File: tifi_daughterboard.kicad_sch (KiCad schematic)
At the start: 16 parts

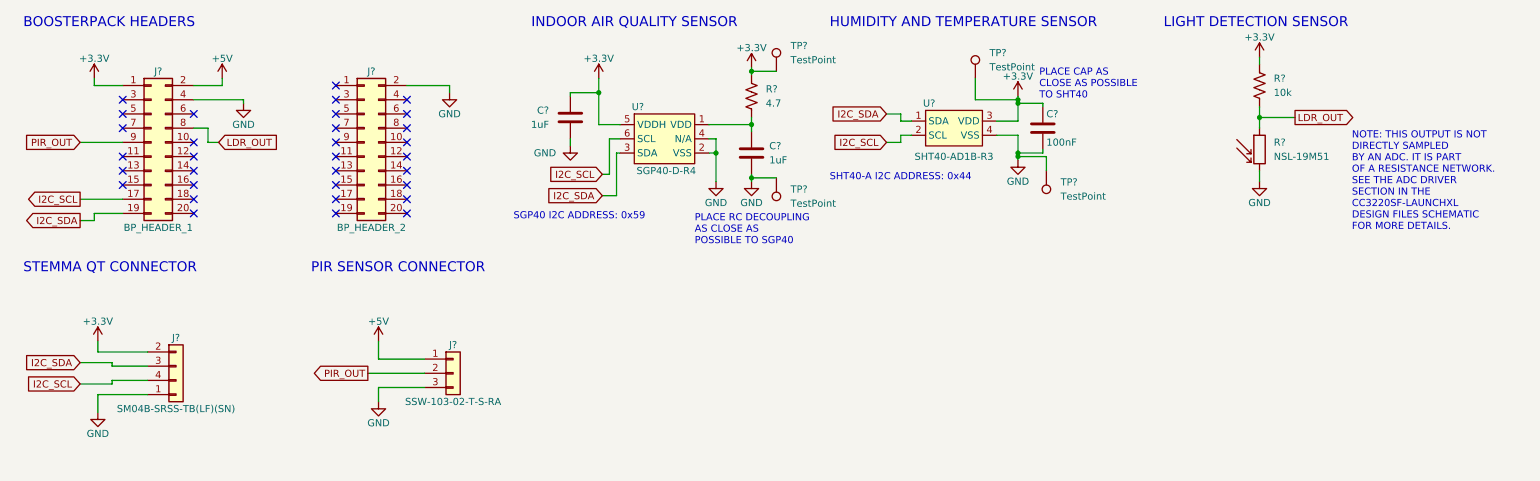
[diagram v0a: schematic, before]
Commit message: Generic cleanup.
Removed test points temporarily until schematic is feature-complete.
Added PWR_FLAG to BoosterPack power pins for ERC check.
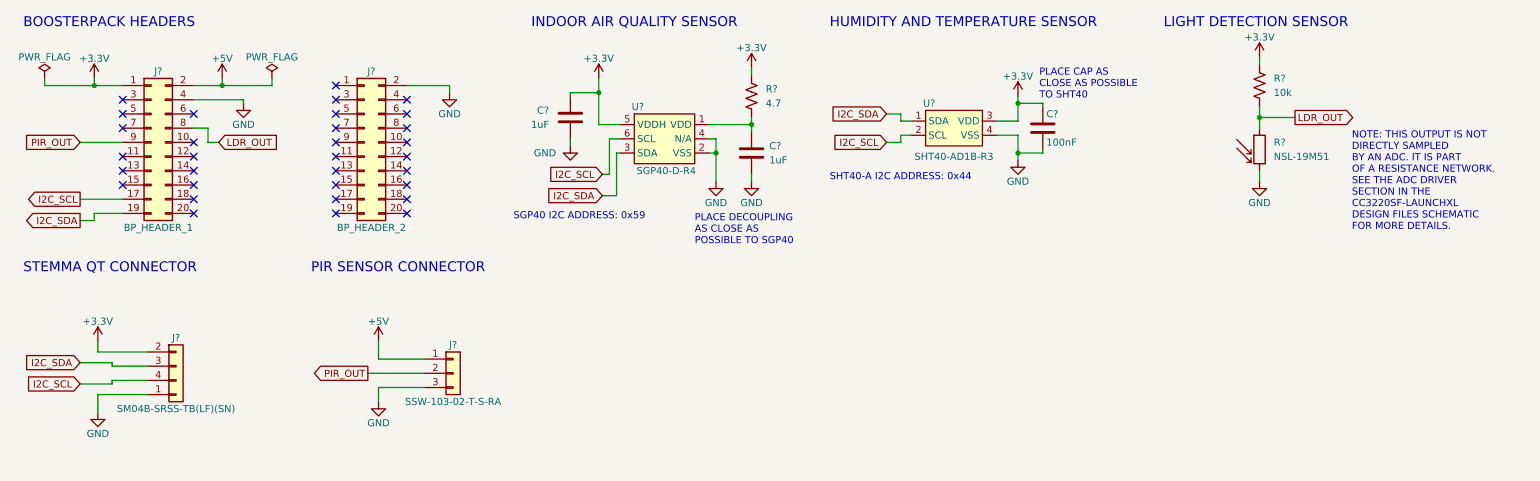
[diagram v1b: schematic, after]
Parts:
- removed TP? (x4): TestPoint, TestPoint:TestPoint_THTPad_1.0x1.0mm_Drill0.5mm, symbol Connector:TestPoint
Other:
- note added: "PLACE DECOUPLING AS CLOSE AS POSSIBLE TO SGP40"
- note removed: "PLACE RC DECOUPLING AS CLOSE AS POSSIBLE TO SGP40"

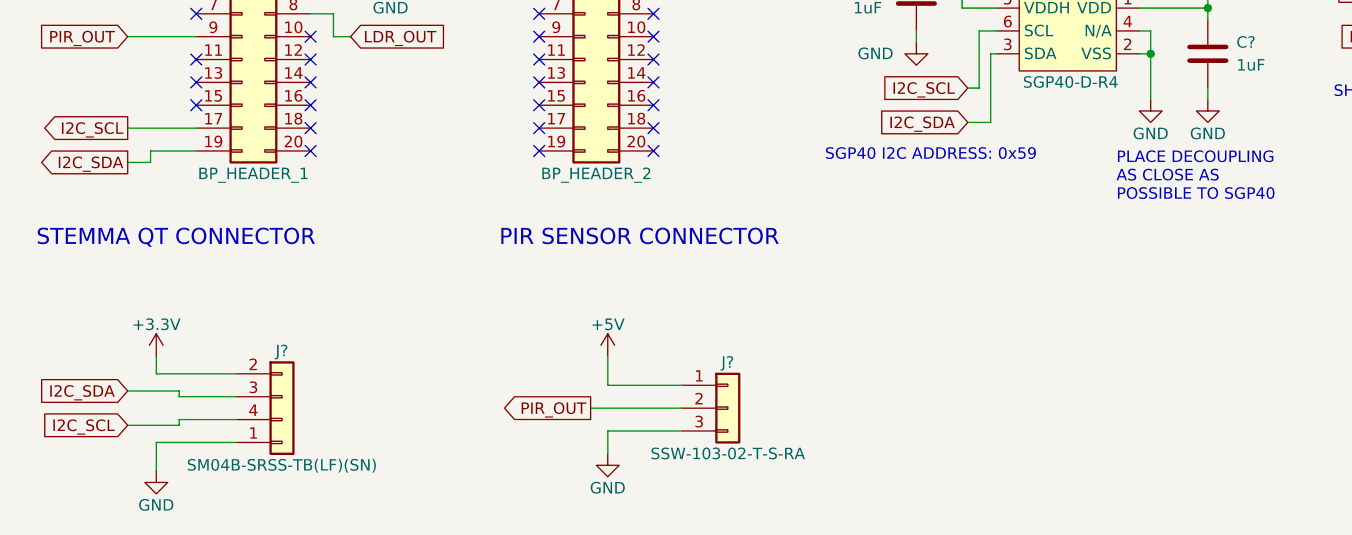
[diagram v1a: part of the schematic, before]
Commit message: Assign parts to BP headers. Add power LED.
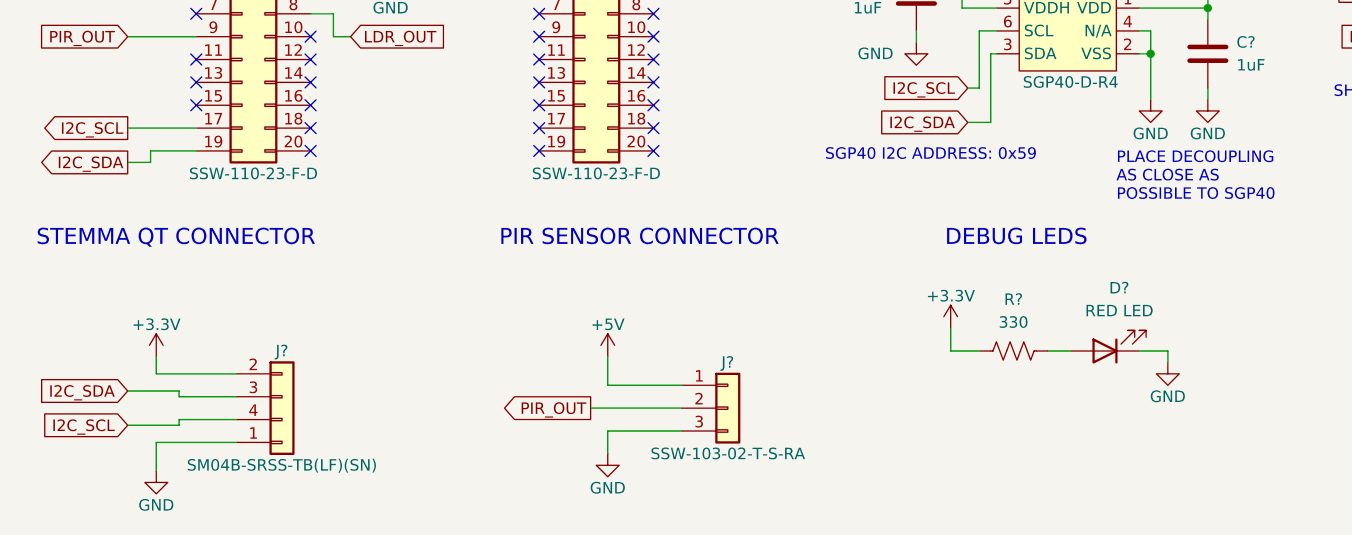
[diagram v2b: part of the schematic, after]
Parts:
- added D?: RED LED, LED_SMD:LED_0805_2012Metric_Pad1.15x1.40mm_HandSolder, symbol Device:LED
- added R?: 330, symbol Device:R_US
- J?: value BP_HEADER_2 -> SSW-110-23-F-D
- J?: value BP_HEADER_1 -> SSW-110-23-F-D
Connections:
- net +3.3V: now also R?.1
- net GND: now also D?.1 (K)
- new net: D?.2 (A), R?.2
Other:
- note added: "DEBUG LEDS"
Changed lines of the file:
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@@
+    (stroke (width 0) (type default) (color 0 0 0 0))
+  )
+  (wire (pts (xy 131.445 75.565) (xy 133.985 75.565))
     (stroke (width 0) (type default) (color 0 0 0 0))
   )
@@
     (stroke (width 0) (type default) (color 0 0 0 0))
   )
+  (wire (pts (xy 120.65 73.025) (xy 120.65 75.565))
+    (stroke (width 0) (type default) (color 0 0 0 0))
+  )
+  (wire (pts (xy 144.78 76.835) (xy 144.78 75.565))
+    (stroke (width 0) (type default) (color 0 0 0 0))
+  )
   (wire (pts (xy 149.225 37.465) (xy 149.225 38.735))
     (stroke (width 0) (type default) (color 0 0 0 0))
@@
     (stroke (width 0) (type default) (color 0 0 0 0))
   )
+  (wire (pts (xy 144.78 75.565) (xy 141.605 75.565))
+    (stroke (width 0) (type default) (color 0 0 0 0))
+  )
   (wire (pts (xy 95.25 31.75) (xy 95.25 30.48))
     (stroke (width 0) (type default) (color 0 0 0 0))
@@
     (stroke (width 0) (type default) (color 0 0 0 0))
   )
+  (wire (pts (xy 120.65 75.565) (xy 123.825 75.565))
+    (stroke (width 0) (type default) (color 0 0 0 0))
+  )
   (wire (pts (xy 95.25 30.48) (xy 87.63 30.48))
     (stroke (width 0) (type default) (color 0 0 0 0))
@@
   (wire (pts (xy 31.75 53.34) (xy 31.75 54.61))
     (stroke (width 0) (type default) (color 0 0 0 0))
+  )
+  (text "DEBUG LEDS" (at 120.015 64.135 0)
+    (effects (font (size 1.778 1.778)) (justify left bottom))
   )
   (text "PLACE DECOUPLING\nAS CLOSE AS\nPOSSIBLE TO SGP40" (at 139.065 59.055 0)
@@
     (in_bom yes) (on_board yes)
     (property "Reference" "J?" (id 0) (at 81.28 27.94 0))
-    (property "Value" "BP_HEADER_2" (id 1) (at 81.28 55.88 0))
+    (property "Value" "SSW-110-23-F-D" (id 1) (at 81.28 55.88 0))
     (property "Footprint" "Connector_PinHeader_2.54mm:PinHeader_2x10_P2.54mm_Vertical" (id 2) (at 80.01 40.64 0)
       (effects (font (size 1.27 1.27)) hide)
@@
     (pin "1")
   )
+  (symbol (lib_id "power:GND") (at 144.78 76.835 0) (unit 1)
+    (in_bom yes) (on_board yes)
+    (property "Reference" "#PWR?" (id 0) (at 144.78 83.185 0)
+      (effects (font (size 1.27 1.27)) hide)
+    )
+    (property "Value" "GND" (id 1) (at 144.78 80.645 0))
+    (property "Footprint" "" (id 2) (at 144.78 76.835 0)
+      (effects (font (size 1.27 1.27)) hide)
+    )
+    (property "Datasheet" "" (id 3) (at 144.78 76.835 0)
+      (effects (font (size 1.27 1.27)) hide)
+    )
+    (pin "1")
+  )
   (symbol (lib_id "power:+3.3V") (at 149.225 27.305 0) (unit 1)
     (in_bom yes) (on_board yes)
@@
     (pin "1")
   )
+  (symbol (lib_id "power:+3.3V") (at 120.65 73.025 0) (unit 1)
+    (in_bom yes) (on_board yes)
+    (property "Reference" "#PWR?" (id 0) (at 120.65 76.835 0)
+      (effects (font (size 1.27 1.27)) hide)
+    )
+    (property "Value" "+3.3V" (id 1) (at 120.65 69.469 0))
+    (property "Footprint" "" (id 2) (at 120.65 73.025 0)
+      (effects (font (size 1.27 1.27)) hide)
+    )
+    (property "Datasheet" "" (id 3) (at 120.65 73.025 0)
+      (effects (font (size 1.27 1.27)) hide)
+    )
+    (pin "1")
+  )
   (symbol (lib_id "power:+3.3V") (at 32.385 76.2 0) (unit 1)
     (in_bom yes) (on_board yes)
@@
     (pin "1")
   )
+  (symbol (lib_id "Device:LED") (at 137.795 75.565 180) (unit 1)
+    (in_bom yes) (on_board yes) (fields_autoplaced)
+    (property "Reference" "D?" (id 0) (at 139.3825 68.58 0))
+    (property "Value" "RED LED" (id 1) (at 139.3825 71.12 0))
+    (property "Footprint" "LED_SMD:LED_0805_2012Metric_Pad1.15x1.40mm_HandSolder" (id 2) (at 137.795 75.565 0)
+      (effects (font (size 1.27 1.27)) hide)
+    )
+    (property "Datasheet" "https://www.we-online.com/katalog/datasheet/150080RS75000.pdf" (id 3) (at 137.795 75.565 0)
+      (effects (font (size 1.27 1.27)) hide)
+    )
+    (pin "1")
+    (pin "2")
+  )
   (symbol (lib_id "Device:C") (at 116.84 36.195 0) (unit 1)
     (in_bom yes) (on_board yes) (fields_autoplaced)
@@
     (in_bom yes) (on_board yes)
     (property "Reference" "J?" (id 0) (at 43.18 27.94 0))
-    (property "Value" "BP_HEADER_1" (id 1) (at 43.18 55.88 0))
+    (property "Value" "SSW-110-23-F-D" (id 1) (at 43.18 55.88 0))
     (property "Footprint" "Connector_PinHeader_2.54mm:PinHeader_2x10_P2.54mm_Vertical" (id 2) (at 41.91 40.64 0)
       (effects (font (size 1.27 1.27)) hide)
@@
     (pin "9")
   )
+  (symbol (lib_id "Device:R_US") (at 127.635 75.565 90) (unit 1)
+    (in_bom yes) (on_board yes) (fields_autoplaced)
+    (property "Reference" "R?" (id 0) (at 127.635 69.85 90))
+    (property "Value" "330" (id 1) (at 127.635 72.39 90))
+    (property "Footprint" "" (id 2) (at 127.889 74.549 90)
+      (effects (font (size 1.27 1.27)) hide)
+    )
+    (property "Datasheet" "~" (id 3) (at 127.635 75.565 0)
+      (effects (font (size 1.27 1.27)) hide)
+    )
+    (pin "1")
+    (pin "2")
+  )
   (symbol (lib_id "Device:R_Photo") (at 240.03 41.91 0) (unit 1)
     (in_bom yes) (on_board yes) (fields_autoplaced)
@@
       (reference "#PWR0117") (unit 1) (value "+3.3V") (footprint "")
     )
+    (path "/36824472-171f-47e6-8702-90b63624dec1"
+      (reference "#PWR?") (unit 1) (value "GND") (footprint "")
+    )
+    (path "/5640c9ba-54bc-43ba-b468-0270cb7170fa"
+      (reference "#PWR?") (unit 1) (value "+3.3V") (footprint "")
+    )
     (path "/7d97e865-7860-4bff-9e38-c39efb9297b4"
       (reference "#PWR?") (unit 1) (value "+5V") (footprint "")
@@
       (reference "C?") (unit 1) (value "1uF") (footprint "")
     )
+    (path "/c6c05906-684a-4ea4-8501-9bf3dd4b9c99"
+      (reference "D?") (unit 1) (value "RED LED") (footprint "LED_SMD:LED_0805_2012Metric_Pad1.15x1.40mm_HandSolder")
+    )
     (path "/03e73a6c-6a66-4743-9386-abd83f09d2a2"
-      (reference "J?") (unit 1) (value "BP_HEADER_2") (footprint "Connector_PinHeader_2.54mm:PinHeader_2x10_P2.54mm_Vertical")
+      (reference "J?") (unit 1) (value "SSW-110-23-F-D") (footprint "Connector_PinHeader_2.54mm:PinHeader_2x10_P2.54mm_Vertical")
     )
     (path "/06a20ec0-9dac-456c-8d69-b314df94801c"
@@
     )
     (path "/eec51399-1c9c-497c-8d0a-e34cae999a37"
-      (reference "J?") (unit 1) (value "BP_HEADER_1") (footprint "Connector_PinHeader_2.54mm:PinHeader_2x10_P2.54mm_Vertical")
+      (reference "J?") (unit 1) (value "SSW-110-23-F-D") (footprint "Connector_PinHeader_2.54mm:PinHeader_2x10_P2.54mm_Vertical")
     )
     (path "/71672d3b-4690-4212-bfa4-42f5ad120dbb"
@@
       (reference "R?") (unit 1) (value "10k") (footprint "")
     )
+    (path "/f1ede1c9-4507-494d-9d3c-c58508b0d150"
+      (reference "R?") (unit 1) (value "330") (footprint "")
+    )
     (path "/f5356d0d-ea25-437c-9f9a-3a02cfee54ec"

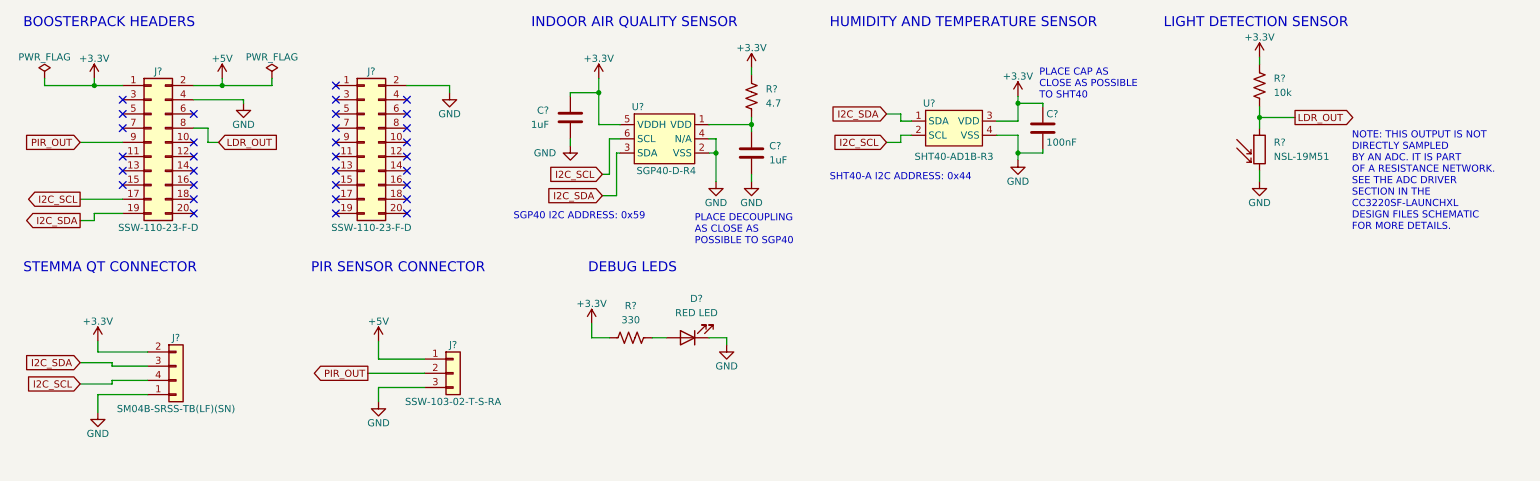
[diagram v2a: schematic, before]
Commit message: Add indicator LED circuit.
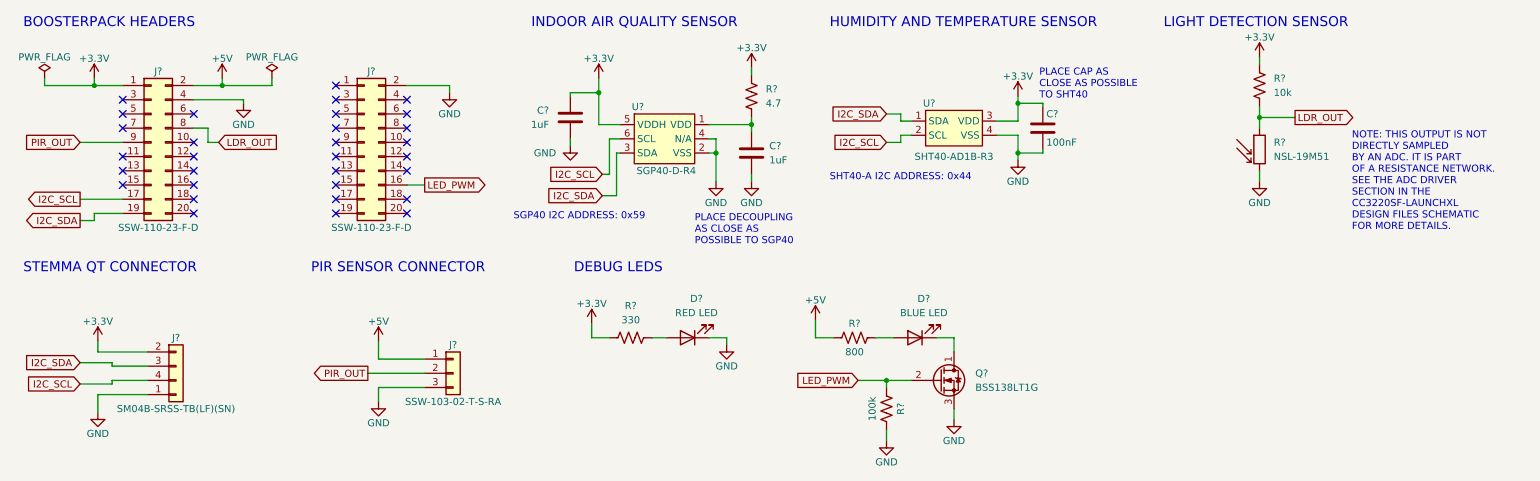
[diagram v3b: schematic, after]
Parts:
- added D?: BLUE LED, LED_SMD:LED_0805_2012Metric_Pad1.15x1.40mm_HandSolder, symbol Device:LED
- added Q?: BSS138LT1G, symbol Device:Q_NMOS_DGS
- added R?: 100k, symbol Device:R_US
- added R?: 800, symbol Device:R_US
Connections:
- net +5V: now also R?.1
- net GND: now also Q?.3 (S), R?.2
- net LED_PWM: now reaches J?.16 (Pin_16)
- net LED_PWM: now also Q?.2 (G), R?.1
- new net: D?.2 (A), R?.2
- new net: D?.1 (K), Q?.1 (D)
- no-connect marks 32 -> 31

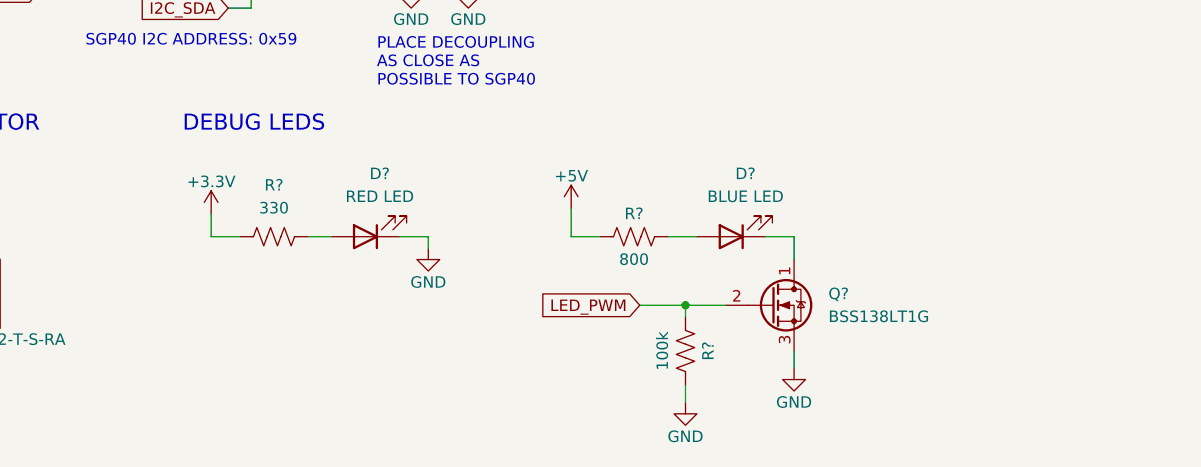
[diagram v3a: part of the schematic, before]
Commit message: Add series gate resistor to LED PWM circuit.
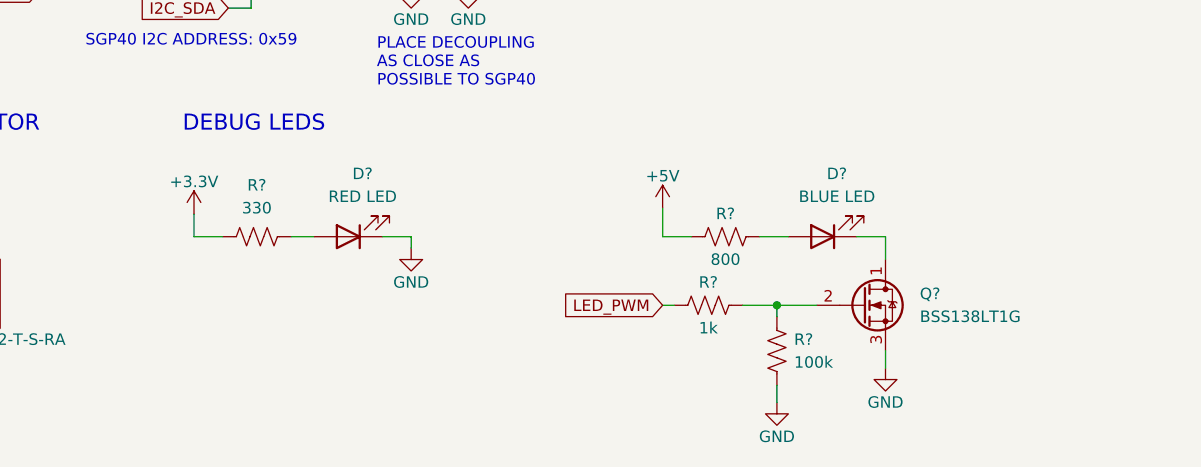
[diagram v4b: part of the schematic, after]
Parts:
- added R?: 1k, symbol Device:R_US
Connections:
- net LED_PWM: now also R?.1; no longer Q?.2 (G), R?.1
- new net: Q?.2 (G), R?.1, R?.2
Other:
- moved on the sheet: D?, Q?, R?

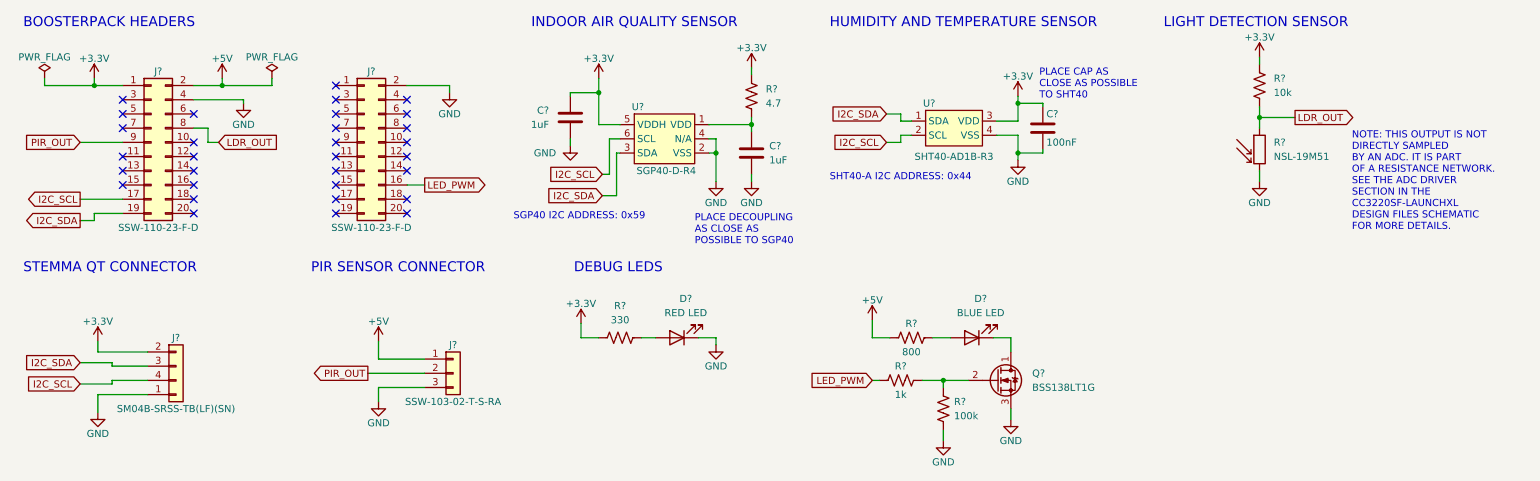
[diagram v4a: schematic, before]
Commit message: Annotate schematic references
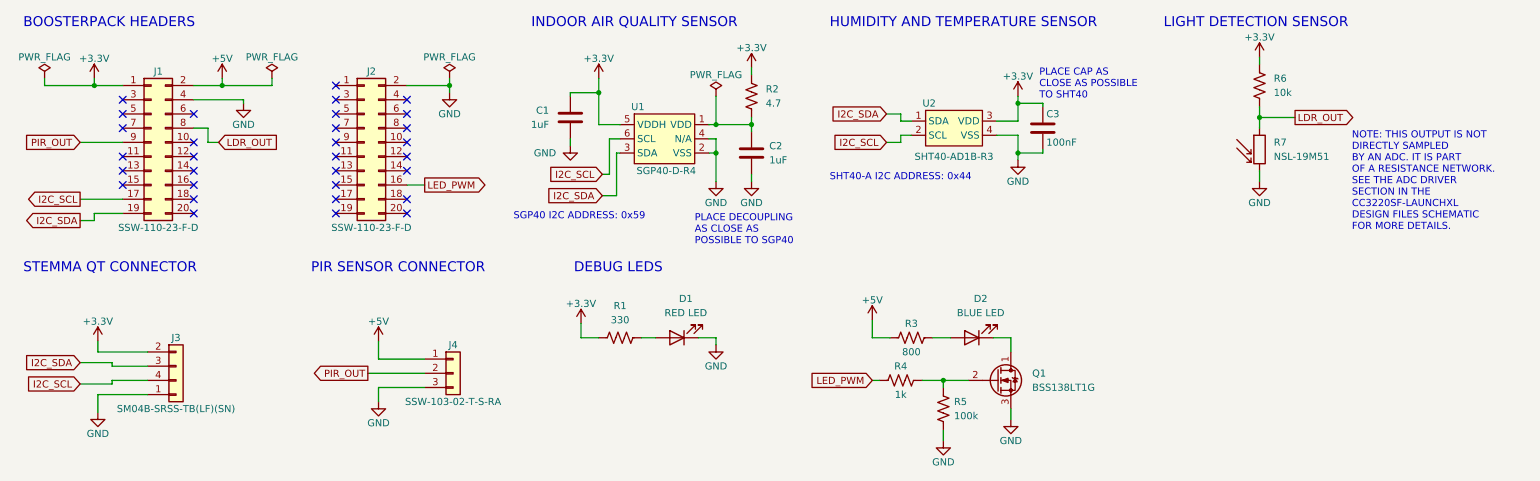
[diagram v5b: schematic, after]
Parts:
- gave numbers to parts that had none: 19
